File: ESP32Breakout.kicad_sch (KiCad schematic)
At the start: 7 parts, among them U1 ESP32-S3

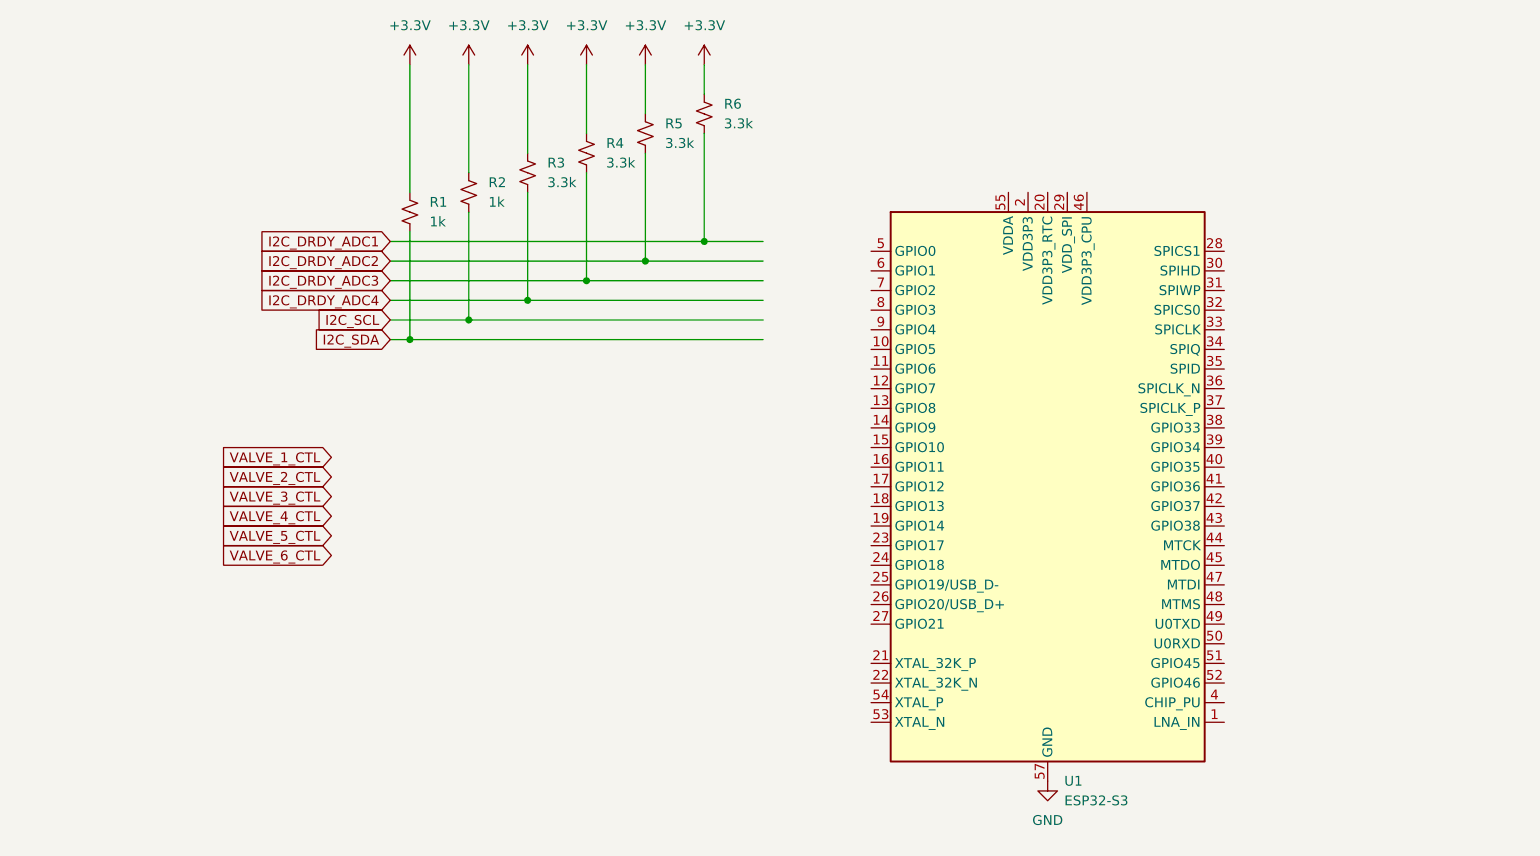
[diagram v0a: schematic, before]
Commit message: Add load cell inputs
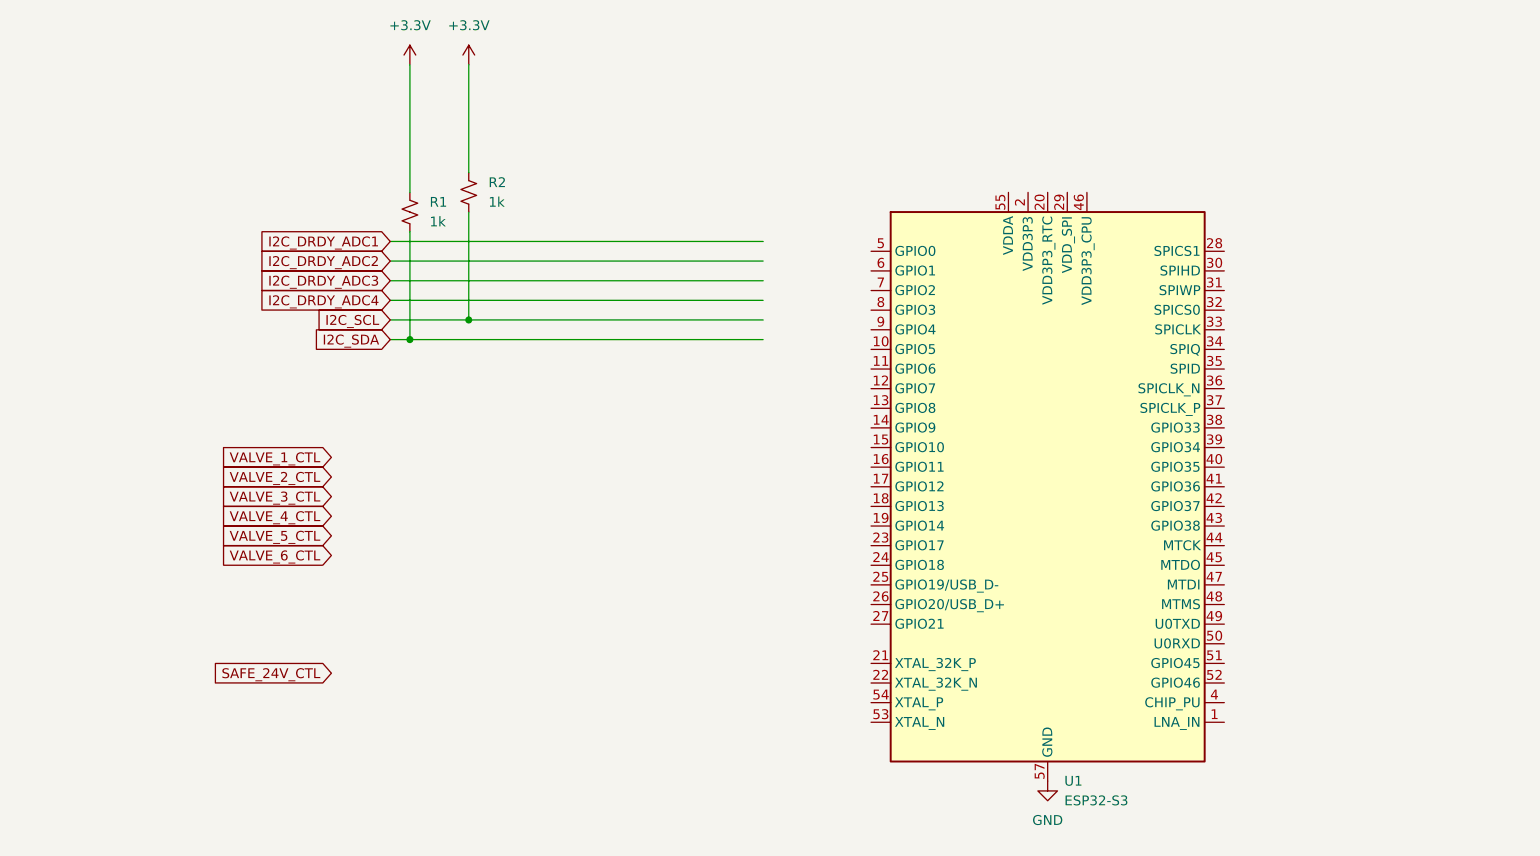
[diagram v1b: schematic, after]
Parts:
- removed R3, R4, R5, R6: 3.3k, Resistor_SMD:R_0402_1005Metric, symbol Device:R_Small_US

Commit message: v0.1 sch. Add devkit c1 footprint
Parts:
- removed U1: ESP32-S3, Package_DFN_QFN:QFN-56-1EP_7x7mm_P0.4mm_EP4x4mm, symbol MCU_Espressif:ESP32-S3
- added J20: PIN6-9_Breakout, TerminalBlock:TerminalBlock_Xinya_XY308-2.54-4P_1x04_P2.54mm_Horizontal, symbol Connector:Screw_Terminal_01x04
- added J21: PIN10-13_Breakout, TerminalBlock:TerminalBlock_Xinya_XY308-2.54-4P_1x04_P2.54mm_Horizontal, symbol Connector:Screw_Terminal_01x04
- added U1: ESP32-S3, Library:ESP32_Devkit_C1_Noah, symbol ESP32_Devkit_C1_Noah:ESP32-S3
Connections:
- net GND: now also U1.GND1 (GND), U1.GND2 (GND), U1.GND3 (GND), U1.GND4 (GND)
- net I2C_DRDY_ADC1: now also U1.2 (GPIO2)
- net I2C_DRDY_ADC2: now also U1.3 (GPIO3)
- net I2C_DRDY_ADC3: now also U1.4 (GPIO4)
- net I2C_DRDY_ADC4: now also U1.5 (GPIO5)
- net I2C_SCL: now also U1.0 (GPIO0)
- net I2C_SDA: now also U1.1 (GPIO1)
- net SAFE_24V_CTL: now also U1.44 (GPIO44)
- net VALVE_1_CTL: now also U1.38 (GPIO38)
- net VALVE_2_CTL: now also U1.39 (GPIO39)
- net VALVE_3_CTL: now also U1.40 (GPIO41)
- net VALVE_4_CTL: now also U1.40 (GPIO41)
- net VALVE_5_CTL: now also U1.42 (GPIO42)
- net VALVE_6_CTL: now also U1.43 (GPIO43)
- new net +5V: U1.5V (5VIN)
- new net IGNITOR_CTL: U1.45 (GPIO45)
- new net PIN10_BREAKOUT: J21.1 (Pin_1), U1.10 (GPIO10)
- new net PIN11_BREAKOUT: J21.2 (Pin_2), U1.11 (GPIO11)
- new net PIN12_BREAKOUT: J21.3 (Pin_3), U1.12 (GPIO12)
- new net PIN13_BREAKOUT: J21.4 (Pin_4), U1.13 (GPIO13)
- new net PIN6_BREAKOUT: J20.1 (Pin_1), U1.6 (GPIO6)
- new net PIN7_BREAKOUT: J20.2 (Pin_2), U1.7 (GPIO7)
- new net PIN8_BREAKOUT: J20.3 (Pin_3), U1.8 (GPIO8)
- new net PIN9_BREAKOUT: J20.4 (Pin_4), U1.9 (GPIO9)
- no-connect marks 0 -> 3
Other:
- moved on the sheet: R1, R2

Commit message: Almost done routing
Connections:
- net I2C_DRDY_ADC1: now also U1.4 (GPIO4); no longer U1.2 (GPIO2)
- net I2C_DRDY_ADC2: now also U1.5 (GPIO5); no longer U1.3 (GPIO3)
- net I2C_DRDY_ADC3: now also U1.6 (GPIO6); no longer U1.4 (GPIO4)
- net I2C_DRDY_ADC4: now also U1.7 (GPIO7); no longer U1.5 (GPIO5)
- net IGNITOR_CTL: now also U1.47 (GPIO47); no longer U1.45 (GPIO45)
- net PIN8_BREAKOUT: now also J20.1 (Pin_1); no longer J20.3 (Pin_3)
- net SAFE_24V_CTL: now also U1.48 (GPIO48); no longer U1.44 (GPIO44)
- net VALVE_4_CTL: now also U1.41 (GPIO41); no longer U1.40 (GPIO41)
- net VALVE_6_CTL: now also U1.2 (GPIO2); no longer U1.43 (GPIO43)
- net PIN46_BREAKOUT: now reaches U1.46 (GPIO46)
- net PIN46_BREAKOUT: now also J20.3 (Pin_3)
- removed net PIN6_BREAKOUT: J20.1 (Pin_1), U1.6 (GPIO6)
- net PIN7_BREAKOUT renamed PIN3_BREAKOUT
- net PIN3_BREAKOUT: now also U1.3 (GPIO3); no longer U1.7 (GPIO7)
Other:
- moved on the sheet: J20

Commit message: routing broken
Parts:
- U1: footprint Library:ESP32_Devkit_C1_Noah -> Package_DFN_QFN:QFN-56-1EP_7x7mm_P0.4mm_EP4x4mm
- renumbered J20 to J1, J21 to J2
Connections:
- net VALVE_4_CTL: now also U1.40 (GPIO41); no longer U1.41 (GPIO41)
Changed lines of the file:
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@@
 		(dnp no)
 		(fields_autoplaced yes)
-		(property "Reference" "#PWR024"
+		(property "Reference" "#PWR01"
 			(at 96.52 40.64 0)
 			(effects
@@
 			(project "nexus"
 				(path "/226c5870-4123-4efa-a2b3-b42d02f59bb7/e5160962-f32b-431d-bdd1-4f3137fc161d"
-					(reference "#PWR024")
+					(reference "#PWR01")
 					(unit 1)
 				)
@@
 		(dnp no)
 		(fields_autoplaced yes)
-		(property "Reference" "#PWR0100"
+		(property "Reference" "#PWR03"
 			(at 137.16 40.64 0)
 			(effects
@@
 			(project ""
 				(path "/226c5870-4123-4efa-a2b3-b42d02f59bb7/e5160962-f32b-431d-bdd1-4f3137fc161d"
-					(reference "#PWR0100")
+					(reference "#PWR03")
 					(unit 1)
 				)
@@
 		(on_board yes)
 		(dnp no)
-		(property "Reference" "J21"
+		(property "Reference" "J2"
 			(at 91.694 83.058 0)
 			(effects
@@
 			(project "nexus"
 				(path "/226c5870-4123-4efa-a2b3-b42d02f59bb7/e5160962-f32b-431d-bdd1-4f3137fc161d"
-					(reference "J21")
+					(reference "J2")
 					(unit 1)
 				)
@@
 		(dnp no)
 		(fields_autoplaced yes)
-		(property "Reference" "#PWR01"
+		(property "Reference" "#PWR04"
 			(at 142.24 130.81 0)
 			(effects
@@
 			(project "nexus"
 				(path "/226c5870-4123-4efa-a2b3-b42d02f59bb7/e5160962-f32b-431d-bdd1-4f3137fc161d"
-					(reference "#PWR01")
+					(reference "#PWR04")
 					(unit 1)
 				)
@@
 			)
 		)
-		(property "Footprint" "Library:ESP32_Devkit_C1_Noah"
+		(property "Footprint" "Package_DFN_QFN:QFN-56-1EP_7x7mm_P0.4mm_EP4x4mm"
 			(at 142.748 134.112 0)
 			(effects
@@
 		(pin "3V3_1"
 		)
-		(pin "41"
+		(pin "40"
 		)
 		(pin "40"
@@
 		(on_board yes)
 		(dnp no)
-		(property "Reference" "J20"
+		(property "Reference" "J1"
 			(at 39.624 33.528 0)
 			(effects
@@
 			(project "nexus"
 				(path "/226c5870-4123-4efa-a2b3-b42d02f59bb7/e5160962-f32b-431d-bdd1-4f3137fc161d"
-					(reference "J20")
-					(unit 1)
-				)
+					(reference "J1")
+					(unit 1)
+				)

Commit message: Fix connector references
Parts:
- U1: footprint Package_DFN_QFN:QFN-56-1EP_7x7mm_P0.4mm_EP4x4mm -> Library:ESP32_Devkit_C1_Noah
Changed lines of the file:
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@@
 			)
 		)
-		(property "Footprint" "Package_DFN_QFN:QFN-56-1EP_7x7mm_P0.4mm_EP4x4mm"
+		(property "Footprint" "Library:ESP32_Devkit_C1_Noah"
 			(at 142.748 134.112 0)
 			(effects

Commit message: Satisfy DRC
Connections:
- net I2C_SCL: now also U1.16 (GPIO16/XTAL_32K_N); no longer U1.0 (GPIO0)
- net I2C_SDA: now also U1.15 (GPIO15/XTAL_32K_P); no longer U1.1 (GPIO1)
- net IGNITOR_CTL: now also U1.39 (GPIO39); no longer U1.47 (GPIO47)
- net SAFE_24V_CTL: now also U1.40 (GPIO40); no longer U1.48 (GPIO48)
- net VALVE_1_CTL: now also U1.43 (GPIO43); no longer U1.38 (GPIO38)
- net VALVE_2_CTL: now also U1.44 (GPIO44); no longer U1.39 (GPIO39)
- net VALVE_3_CTL: now also U1.1 (GPIO1); no longer U1.40 (GPIO41)
- net VALVE_4_CTL: now also U1.2 (GPIO2); no longer U1.40 (GPIO41)
- net VALVE_6_CTL: now also U1.41 (GPIO41); no longer U1.2 (GPIO2)
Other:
- moved on the sheet: R1, R2

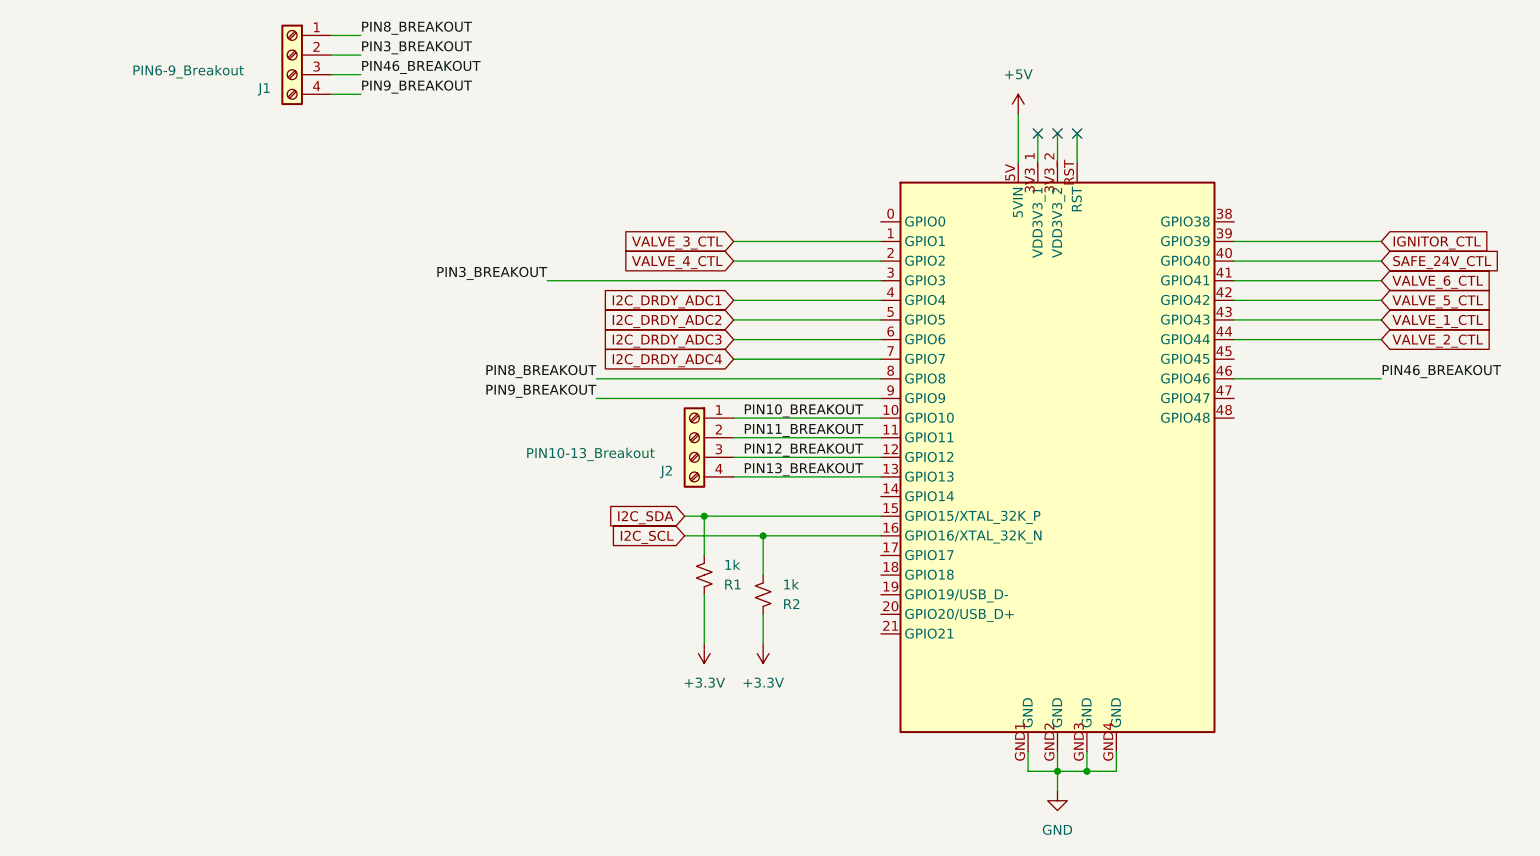
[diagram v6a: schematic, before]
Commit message: Fix silk screening
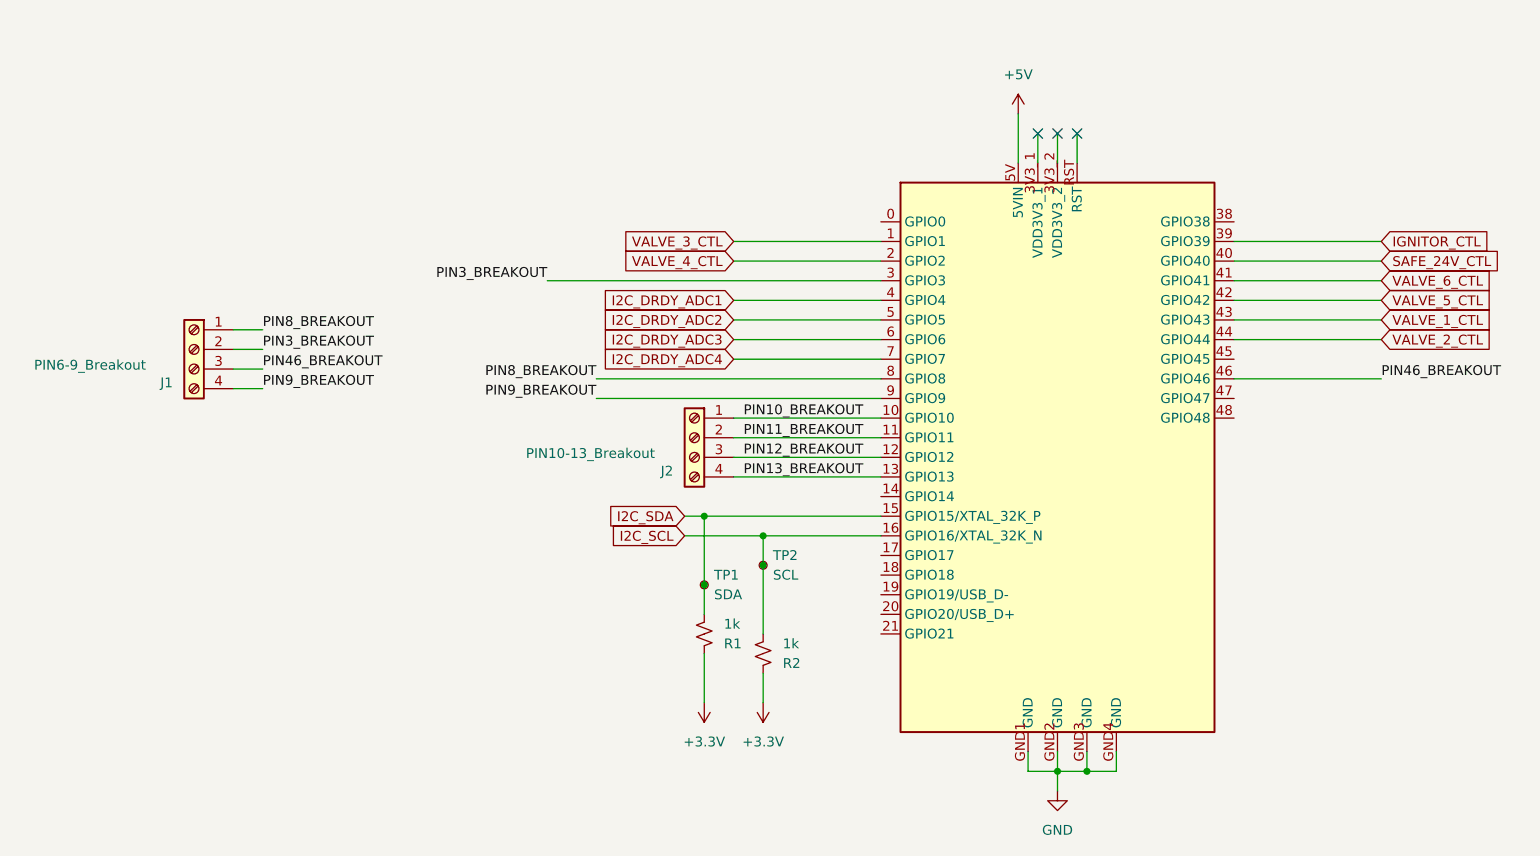
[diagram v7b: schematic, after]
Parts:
- added TP1: SDA, TestPoint:TestPoint_Pad_D1.5mm, symbol Connector:TestPoint_Small
- added TP2: SCL, TestPoint:TestPoint_Pad_D1.5mm, symbol Connector:TestPoint_Small
- J1, U1: now left out of the parts list
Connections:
- net I2C_SCL: now also TP2.1
- net I2C_SDA: now also TP1.1
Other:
- moved on the sheet: J1, R1, R2
